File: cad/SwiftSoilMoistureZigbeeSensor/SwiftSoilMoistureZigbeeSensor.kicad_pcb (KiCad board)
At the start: 2 copper layers, 83.8 x 22.9 mm, 13 parts, among them J1 Probe, J2 BAT, J3 ARM SWD 10, Q1 BSS84, SW1 Factory Reset, U1 TPS61221DCK, U2 E73-2G4M08S1C

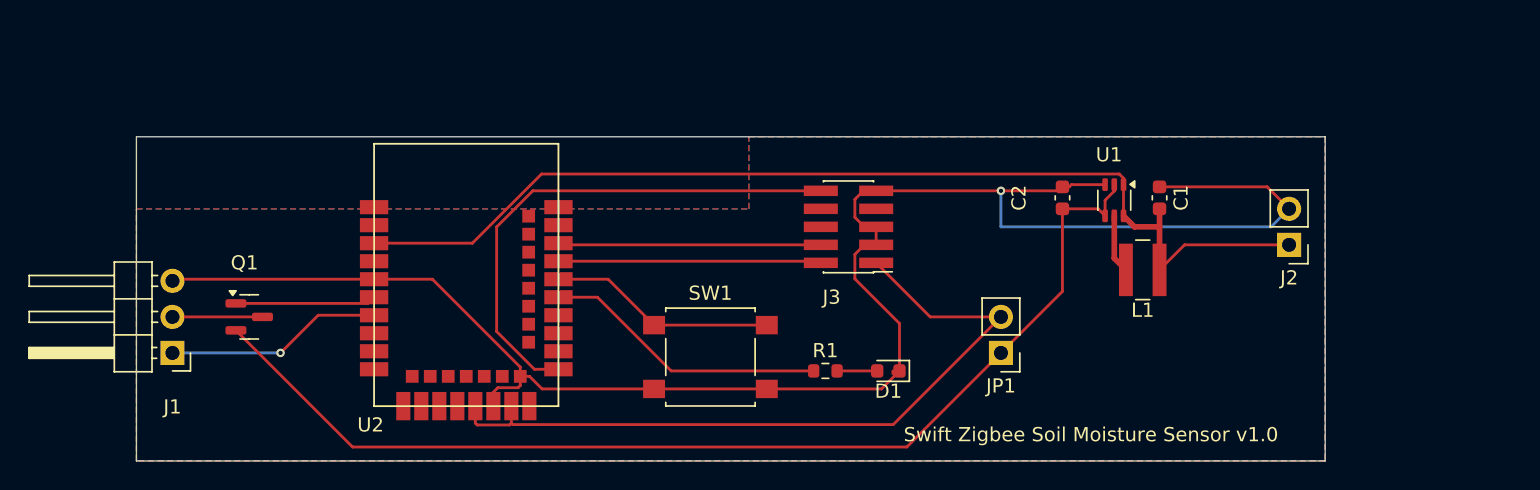
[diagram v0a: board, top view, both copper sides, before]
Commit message: Changed SWD connector
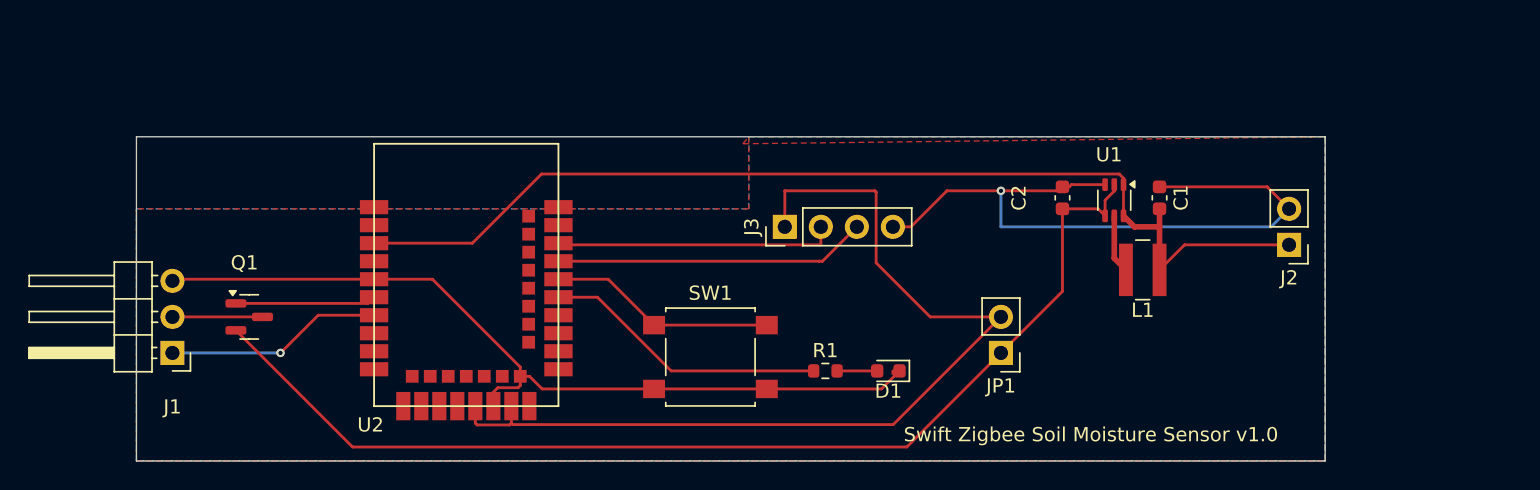
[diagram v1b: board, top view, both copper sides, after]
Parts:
- J3: value ARM SWD 10 -> ARM SWD; footprint Connector_PinHeader_1.27mm:PinHeader_2x05_P1.27mm_Vertical_SMD -> Connector_PinHeader_2.54mm:PinHeader_1x04_P2.54mm_Vertical
- moved J3 4.49 mm to (109.2, 57.1), turned to 90 degrees
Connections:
- J3 pad 2: Net-(J3-SWDIO/TMS) -> Net-(J3-SWDCLK)
- J3 pad 3: GND -> Net-(J3-SWDIO)
- J3 pad 4: Net-(J3-SWCLK/TCK) -> GND
- U2 pad 26: Net-(J3-~{RESET}) -> unconnected-(U2A-P0.18/RESET-Pad26)
- U2 pad 37: Net-(J3-SWDIO/TMS) -> Net-(J3-SWDIO)
- U2 pad 39: Net-(J3-SWCLK/TCK) -> Net-(J3-SWDCLK)
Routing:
- net Net-(J3-~{RESET}): track 36.7 -> 0.00 mm
- net Net-(J3-SWDIO): track 0.00 -> 23.0 mm
- net Net-(J3-SWDCLK): track 0.00 -> 19.8 mm
- net Net-(J3-SWCLK/TCK): track 18.6 -> 0.00 mm
- net Net-(J3-SWDIO/TMS): track 18.6 -> 0.00 mm
- net GND: track 126.4 -> 108.9 mm
- net +3.3V: track 53.1 -> 67.1 mm

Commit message: Rewworked SWD connector
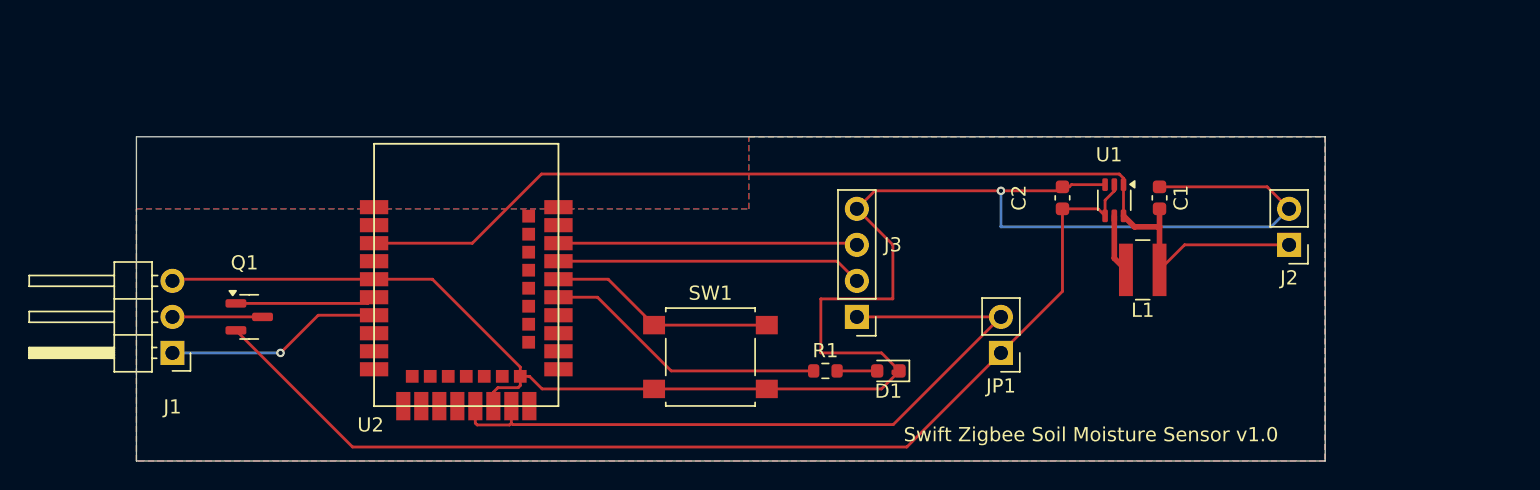
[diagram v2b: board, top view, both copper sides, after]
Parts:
- moved J3 8.13 mm to (114.3, 63.5), turned to 180 degrees
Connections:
- J3 pad 2: Net-(J3-SWDCLK) -> Net-(J3-SWDIO)
- J3 pad 3: Net-(J3-SWDIO) -> Net-(J3-SWDCLK)
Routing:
- net GND: track 108.9 -> 133.3 mm
- net +3.3V: track 67.1 -> 52.9 mm
- net Net-(J3-SWDCLK): track 19.8 -> 21.3 mm
- net Net-(J3-SWDIO): track 23.0 -> 21.6 mm
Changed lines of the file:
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@@
   )
   (footprint "Connector_PinHeader_2.54mm:PinHeader_1x04_P2.54mm_Vertical" (layer "F.Cu")
-    (at 109.22 57.15 90)
+    (at 114.3 63.5 180)
     (descr "Through hole straight pin header, 1x04, 2.54mm pitch, single row")
     (tags "Through hole pin header THT 1x04 2.54mm single row")
@@
     (property "ki_keywords" "connector")
     (attr through_hole)
-    (fp_text reference "J3" (at 0 -2.33 90) (layer "F.SilkS")
-        (effects (font (size 1 1) (thickness 0.15)))
-    )
-    (fp_text value "ARM SWD" (at -3.81 3.81 180) (layer "F.Fab")
-        (effects (font (size 1 1) (thickness 0.15)))
-    )
-    (fp_text user "${REFERENCE}" (at 0 3.81) (layer "F.Fab")
+    (fp_text reference "J3" (at -2.54 5.08) (layer "F.SilkS")
+        (effects (font (size 1 1) (thickness 0.15)))
+    )
+    (fp_text value "ARM SWD" (at 0 11.43) (layer "F.Fab")
+        (effects (font (size 1 1) (thickness 0.15)))
+    )
+    (fp_text user "${REFERENCE}" (at 0 3.81 90) (layer "F.Fab")
         (effects (font (size 1 1) (thickness 0.15)))
     )
@@
     (fp_line (start 1.27 8.89) (end -1.27 8.89)
       (stroke (width 0.1) (type solid)) (layer "F.Fab"))
-    (pad "1" thru_hole rect (at 0 0 90) (size 1.7 1.7) (drill 1) (layers "*.Cu" "*.Mask")
+    (pad "1" thru_hole rect (at 0 0 180) (size 1.7 1.7) (drill 1) (layers "*.Cu" "*.Mask")
       (net 3 "+3.3V") (pinfunction "Vtref") (pintype "power_in"))
-    (pad "2" thru_hole oval (at 0 2.54 90) (size 1.7 1.7) (drill 1) (layers "*.Cu" "*.Mask")
+    (pad "2" thru_hole oval (at 0 2.54 180) (size 1.7 1.7) (drill 1) (layers "*.Cu" "*.Mask")
+      (net 43 "Net-(J3-SWDIO)") (pinfunction "SWDIO") (pintype "bidirectional"))
+    (pad "3" thru_hole oval (at 0 5.08 180) (size 1.7 1.7) (drill 1) (layers "*.Cu" "*.Mask")
       (net 42 "Net-(J3-SWDCLK)") (pinfunction "SWDCLK") (pintype "input"))
-    (pad "3" thru_hole oval (at 0 5.08 90) (size 1.7 1.7) (drill 1) (layers "*.Cu" "*.Mask")
-      (net 43 "Net-(J3-SWDIO)") (pinfunction "SWDIO") (pintype "bidirectional"))
-    (pad "4" thru_hole oval (at 0 7.62 90) (size 1.7 1.7) (drill 1) (layers "*.Cu" "*.Mask")
+    (pad "4" thru_hole oval (at 0 7.62 180) (size 1.7 1.7) (drill 1) (layers "*.Cu" "*.Mask")
       (net 2 "GND") (pinfunction "GND") (pintype "power_in"))
     (model "${KICAD6_3DMODEL_DIR}/Connector_PinHeader_2.54mm.3dshapes/PinHeader_1x04_P2.54mm_Vertical.wrl"
@@
   (segment (start 133.1025 54.175) (end 133.1025 56.375) (width 0.2) (layer "F.Cu") (net 1))
   (segment (start 133.8775 57.15) (end 135.6425 57.15) (width 0.4) (layer "F.Cu") (net 1))
+  (segment (start 116.84 58.42) (end 114.3 55.88) (width 0.2) (layer "F.Cu") (net 2))
   (segment (start 128.7975 54.33) (end 129.2725 54.33) (width 0.2) (layer "F.Cu") (net 2))
+  (segment (start 117.3075 67.31) (end 116.0375 66.04) (width 0.2) (layer "F.Cu") (net 2))
   (segment (start 117.3075 67.31) (end 116.0375 68.58) (width 0.2) (layer "F.Cu") (net 2))
   (segment (start 91.2175 67.6935) (end 90.5675 67.6935) (width 0.2) (layer "F.Cu") (net 2))
@@
   (segment (start 92.104 68.58) (end 91.2175 67.6935) (width 0.2) (layer "F.Cu") (net 2))
   (segment (start 129.2725 54.33) (end 129.4275 54.175) (width 0.2) (layer "F.Cu") (net 2))
+  (segment (start 115.57 54.61) (end 114.3 55.88) (width 0.2) (layer "F.Cu") (net 2))
   (segment (start 90.5675 68.3435) (end 90.4175 68.4935) (width 0.2) (layer "F.Cu") (net 2))
   (segment (start 116.84 67.509999) (end 116.84 67.31) (width 0.2) (layer "F.Cu") (net 2))
   (segment (start 80.141 60.96) (end 80.2575 60.8435) (width 0.2) (layer "F.Cu") (net 2))
   (segment (start 90.5675 67.0435) (end 84.3675 60.8435) (width 0.2) (layer "F.Cu") (net 2))
-  (segment (start 118.11 57.15) (end 116.84 57.15) (width 0.2) (layer "F.Cu") (net 2))
+  (segment (start 128.7975 54.33) (end 128.5175 54.61) (width 0.2) (layer "F.Cu") (net 2))
   (segment (start 129.4275 54.175) (end 131.8025 54.175) (width 0.2) (layer "F.Cu") (net 2))
-  (segment (start 120.65 54.61) (end 118.11 57.15) (width 0.2) (layer "F.Cu") (net 2))
-  (segment (start 120.65 54.61) (end 128.5175 54.61) (width 0.2) (layer "F.Cu") (net 2))
+  (segment (start 116.84 62.23) (end 116.84 58.42) (width 0.2) (layer "F.Cu") (net 2))
+  (segment (start 111.76 62.23) (end 116.84 62.23) (width 0.2) (layer "F.Cu") (net 2))
   (segment (start 90.4175 68.4935) (end 88.9865 68.4935) (width 0.2) (layer "F.Cu") (net 2))
+  (segment (start 111.76 66.04) (end 111.76 62.23) (width 0.2) (layer "F.Cu") (net 2))
   (segment (start 100 68.58) (end 92.104 68.58) (width 0.2) (layer "F.Cu") (net 2))
   (segment (start 107.95 68.58) (end 100 68.58) (width 0.2) (layer "F.Cu") (net 2))
@@
   (segment (start 135.6425 54.33) (end 143.23 54.33) (width 0.2) (layer "F.Cu") (net 2))
   (segment (start 143.23 54.33) (end 144.78 55.88) (width 0.2) (layer "F.Cu") (net 2))
-  (segment (start 128.5175 54.61) (end 128.7975 54.33) (width 0.2) (layer "F.Cu") (net 2))
+  (segment (start 128.5175 54.61) (end 115.57 54.61) (width 0.2) (layer "F.Cu") (net 2))
+  (segment (start 116.0375 66.04) (end 111.76 66.04) (width 0.2) (layer "F.Cu") (net 2))
   (segment (start 66.1565 60.8435) (end 66.04 60.96) (width 0.2) (layer "F.Cu") (net 2))
   (via (at 124.46 54.61) (size 0.6) (drill 0.3) (layers "F.Cu" "B.Cu") (net 2))
@@
   (segment (start 116.8665 71.0935) (end 90.0375 71.0935) (width 0.2) (layer "F.Cu") (net 3))
   (segment (start 87.524 71.12) (end 87.3975 70.9935) (width 0.2) (layer "F.Cu") (net 3))
+  (segment (start 124.46 63.5) (end 114.3 63.5) (width 0.2) (layer "F.Cu") (net 3))
   (segment (start 89.9375 70.9935) (end 89.811 71.12) (width 0.2) (layer "F.Cu") (net 3))
-  (segment (start 115.57 54.61) (end 109.22 54.61) (width 0.2) (layer "F.Cu") (net 3))
   (segment (start 89.811 71.12) (end 87.524 71.12) (width 0.2) (layer "F.Cu") (net 3))
   (segment (start 124.46 63.5) (end 116.8665 71.0935) (width 0.2) (layer "F.Cu") (net 3))
   (segment (start 89.9375 69.7935) (end 89.9375 70.9935) (width 0.2) (layer "F.Cu") (net 3))
-  (segment (start 119.47 63.5) (end 115.66 59.69) (width 0.2) (layer "F.Cu") (net 3))
   (segment (start 90.0375 71.0935) (end 89.9375 70.9935) (width 0.2) (layer "F.Cu") (net 3))
-  (segment (start 109.22 54.61) (end 109.22 57.15) (width 0.2) (layer "F.Cu") (net 3))
-  (segment (start 115.66 59.69) (end 115.66 54.7) (width 0.2) (layer "F.Cu") (net 3))
-  (segment (start 124.46 63.5) (end 119.47 63.5) (width 0.2) (layer "F.Cu") (net 3))
-  (segment (start 115.66 54.7) (end 115.57 54.61) (width 0.2) (layer "F.Cu") (net 3))
   (segment (start 112.905 67.31) (end 115.7325 67.31) (width 0.2) (layer "F.Cu") (net 4))
   (segment (start 76.3165 63.3835) (end 73.66 66.04) (width 0.2) (layer "F.Cu") (net 5))
@@
   (segment (start 78.74 72.675) (end 117.825 72.675) (width 0.2) (layer "F.Cu") (net 41))
   (segment (start 131.8025 56.375) (end 131.3075 55.88) (width 0.2) (layer "F.Cu") (net 41))
-  (segment (start 111.76 58.42) (end 93.374 58.42) (width 0.2) (layer "F.Cu") (net 42))
+  (segment (start 93.2575 58.3035) (end 114.1835 58.3035) (width 0.2) (layer "F.Cu") (net 42))
+  (segment (start 114.1835 58.3035) (end 114.3 58.42) (width 0.2) (layer "F.Cu") (net 42))
   (segment (start 93.374 58.42) (end 93.2575 58.3035) (width 0.2) (layer "F.Cu") (net 42))
-  (segment (start 111.76 58.42) (end 111.76 57.15) (width 0.2) (layer "F.Cu") (net 42))
-  (segment (start 111.6435 59.5735) (end 93.2575 59.5735) (width 0.2) (layer "F.Cu") (net 43))
-  (segment (start 114.16 56.48) (end 114.83 57.15) (width 0.2) (layer "F.Cu") (net 43))
-  (segment (start 111.8765 59.5735) (end 114.3 57.15) (width 0.2) (layer "F.Cu") (net 43))
-  (segment (start 111.6435 59.5735) (end 111.8765 59.5735) (width 0.2) (layer "F.Cu") (net 43))
+  (segment (start 114.3 60.96) (end 112.9135 59.5735) (width 0.2) (layer "F.Cu") (net 43))
+  (segment (start 112.9135 59.5735) (end 93.2575 59.5735) (width 0.2) (layer "F.Cu") (net 43))
   (zone (net 2) (net_name "GND") (layer "F.Cu") (hatch edge 0.5)
     (connect_pads (clearance 0.2))
@@
     (polygon
       (pts
+        (xy 63.5 55.88)
+        (xy 106.68 55.88)
         (xy 106.68 50.8)
-        (xy 106.68 55.88)
-        (xy 63.5 55.88)
+        (xy 147.32 50.8)
+        (xy 147.32 73.66)
         (xy 63.5 73.66)
-        (xy 147.32 73.66)
-        (xy 147.32 50.8)
-        (xy 106.2575 51.2935)
       )
     )
   )
   (zone (net 2) (net_name "GND") (layer "B.Cu") (hatch edge 0.5)
-    (priority 1)
-    (connect_pads (clearance 0.5))
+    (connect_pads (clearance 0.2))
     (min_thickness 0.25) (filled_areas_thickness no)
     (fill yes (thermal_gap 0.5) (thermal_bridge_width 0.5))

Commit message: Bad LED wiring
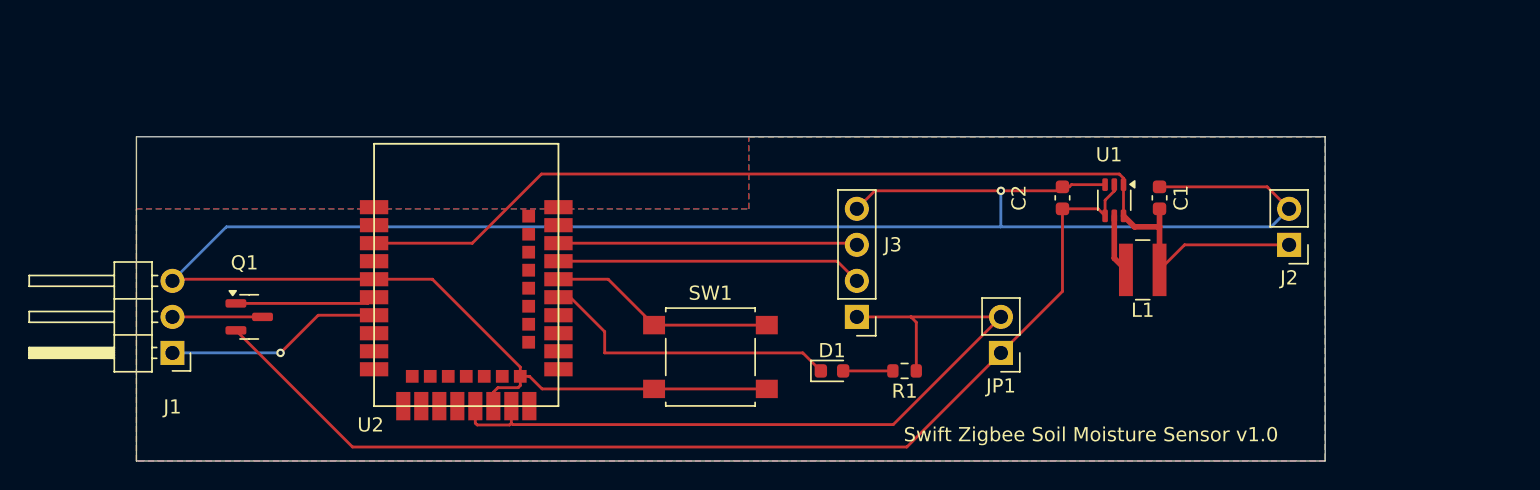
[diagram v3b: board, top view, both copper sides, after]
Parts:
- moved R1 5.59 mm to (117.7, 67.3), turned to 180 degrees
- moved D1 3.97 mm to (112.5, 67.3), turned to 0 degrees
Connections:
- D1 pad 1: GND -> Net-(D1-K)
- R1 pad 1: Net-(U2B-P0.13) -> +3.3V
- U2 pad 33: Net-(U2B-P0.13) -> Net-(D1-K)
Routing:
- net GND: track 133.3 -> 160.8 mm
- net Net-(D1-K): track 0.00 -> 21.7 mm
- net Net-(U2B-P0.13): track 20.3 -> 0.00 mm
- net +3.3V: track 52.9 -> 56.9 mm
- net Net-(D1-A): track 2.83 -> 3.51 mm

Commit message: PCB Version 1.1
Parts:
- removed J2: BAT, Connector_PinHeader_2.54mm:PinHeader_1x02_P2.54mm_Vertical
- added BT1: CR2032, Battery:BatteryHolder_Keystone_1060_1x2032, B.Cu at (141.6, 54.6)
- moved Q1 18.0 mm to (87.3, 54.9)
- moved J1 17.0 mm to (81.3, 58.4)
- moved U2 15.3 mm to (100.2, 53.3)
- moved J3 14.2 mm to (120.7, 50.8), turned to -90 degrees
- moved SW1 13.7 mm to (115.7, 59.4)
- moved D1 12.8 mm to (123.7, 61.0)
- moved R1 12.6 mm to (124.5, 56.7), turned to -90 degrees
- moved C1 9.50 mm to (142.1, 48.1)
- moved U1 9.22 mm to (138.4, 48.3)
- moved C2 9.00 mm to (134.4, 48.1)
- moved L1 8.08 mm to (139.6, 54.0)
- moved JP1 6.35 mm to (128.3, 61.0), turned to 0 degrees
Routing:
- net GND: track 160.8 -> 115.6 mm
- net +3.3V: track 56.9 -> 44.1 mm
- net Net-(J3-SWDCLK): track 21.3 -> 9.83 mm
- net Net-(J3-SWDIO): track 21.6 -> 12.2 mm
- net Net-(JP1-A): track 77.7 -> 85.0 mm
- net Net-(BT1-+): track 74.7 -> 80.6 mm, vias 0 -> 1
- net Net-(Q1-G): track 9.92 -> 7.59 mm
- net Net-(J1-Pin_1): track 15.3 -> 13.4 mm, vias 1 -> 0
- net Net-(D1-K): track 21.7 -> 20.2 mm
- net Net-(U2B-P0.24): track 16.0 -> 14.6 mm
- net Net-(J1-Pin_2): track 6.35 -> 7.35 mm
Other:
- board size 83.8 x 22.9 mm -> 80 x 22.9 mm
- board text added: "Swift Zigbee Soil Moisture Sensor v1.1"
- board text removed: "Swift Zigbee Soil Moisture Sensor v1.0"

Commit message: 680ohm is enough. SWD silk text for convinience
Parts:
- R1: value 220Ω -> 680Ω
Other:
- board text added: "CLK"
- board text added: "GND"
- board text added: "I/O"
- board text added: "Vtref"
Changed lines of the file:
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@@
         (effects (font (size 1 1) (thickness 0.15)))
     )
-    (fp_text value "220Ω" (at 0 1.43 90) (layer "F.Fab") hide
+    (fp_text value "680Ω" (at 0 1.43 90) (layer "F.Fab") hide
         (effects (font (size 1 1) (thickness 0.15)))
     )
@@
     (descr "Through hole angled pin header, 1x03, 2.54mm pitch, 6mm pin length, single row")
     (tags "Through hole angled pin header THT 1x03 2.54mm single row")
-    (property "LCSC" " C7089182")
+    (property "LCSC" "Male C2935928 / Female C7089182")
     (property "Sheetfile" "SwiftSoilMoistureZigbeeSensor.kicad_sch")
     (property "Sheetname" "")
@@
     (descr "Through hole straight pin header, 1x02, 2.54mm pitch, single row")
     (tags "Through hole pin header THT 1x02 2.54mm single row")
-    (property "LCSC" "C180247 + C3715628")
+    (property "LCSC" "C492401 + C3715628")
     (property "Sheetfile" "SwiftSoilMoistureZigbeeSensor.kicad_sch")
     (property "Sheetname" "")
@@
     (descr "Inductor, Wuerth Elektronik, Wuerth_MAPI-4020, 4.0mmx4.0mm")
     (tags "inductor Wuerth smd")
-    (property "LCSC" " C87172")
+    (property "LCSC" "C87172")
     (property "Sheetfile" "SwiftSoilMoistureZigbeeSensor.kicad_sch")
     (property "Sheetname" "")
@@
     (descr "Through hole straight pin header, 1x04, 2.54mm pitch, single row")
     (tags "Through hole pin header THT 1x04 2.54mm single row")
-    (property "LCSC" "")
+    (property "LCSC" "C6332197")
     (property "Sheetfile" "SwiftSoilMoistureZigbeeSensor.kicad_sch")
     (property "Sheetname" "")
@@
     (descr "http://www.keyelco.com/product-pdf.cfm?p=726")
     (tags "CR2032 BR2032 BatteryHolder Battery")
+    (property "LCSC" "C22363833")
     (property "Sheetfile" "SwiftSoilMoistureZigbeeSensor.kicad_sch")
     (property "Sheetname" "")
@@
   (gr_rect (start 78.74 43.18) (end 158.75 66.04)
     (stroke (width 0.05) (type default)) (fill none) (layer "Edge.Cuts"))
+  (gr_text "GND" (at 113.244234 48.784336 90) (layer "F.SilkS")
+    (effects (font (size 0.5 0.5) (thickness 0.1)) (justify left bottom))
+  )
+  (gr_text "I/O" (at 118.365243 48.848497 90) (layer "F.SilkS")
+    (effects (font (size 0.5 0.5) (thickness 0.1)) (justify left bottom))
+  )
+  (gr_text "CLK" (at 115.803547 48.81388 90) (layer "F.SilkS")
+    (effects (font (size 0.5 0.5) (thickness 0.1)) (justify left bottom))
+  )
   (gr_text "Swift Zigbee Soil\nMoisture Sensor v1.1" (at 140.97 64.77) (layer "F.SilkS")
     (effects (font (size 1 1) (thickness 0.1)) (justify left bottom))
   )
+  (gr_text "Vtref" (at 120.909631 48.761953 90) (layer "F.SilkS")
+    (effects (font (size 0.5 0.5) (thickness 0.1)) (justify left bottom))
+  )
   (segment (start 142.845 46.325) (end 142.845 48.105) (width 0.2) (layer "F.Cu") (net 1))
